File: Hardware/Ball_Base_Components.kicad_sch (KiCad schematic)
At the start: 58 parts, among them J1 Eurorack_10_pin_power, J2 SWD_Header, J3 USB_B_Micro, J4 X_Out, J5 Y_Out, J6 Z_Out, U1 STM32WB35, U3 LD1117-3.3-4Tab, U4 TL072, U5 TL074, Y2 32MHz

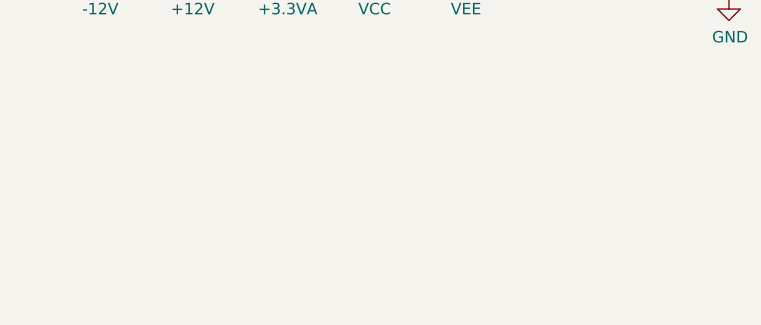
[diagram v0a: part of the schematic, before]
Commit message: Base PCB Updates and resize
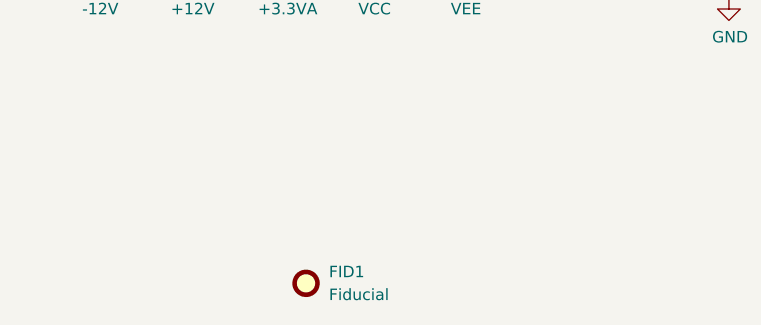
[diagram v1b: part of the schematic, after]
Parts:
- added FID1: Fiducial, Custom_Footprints:4_Layer_Markers, symbol Mechanical:Fiducial
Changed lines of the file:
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@@
     (pin "2")
+  )
+  (symbol (lib_id "Mechanical:Fiducial") (at 44.45 236.22 0) (unit 1)
+    (in_bom yes) (on_board yes) (fields_autoplaced)
+    (property "Reference" "FID1" (id 0) (at 46.99 234.9499 0)
+      (effects (font (size 1.27 1.27)) (justify left))
+    )
+    (property "Value" "Fiducial" (id 1) (at 46.99 237.4899 0)
+      (effects (font (size 1.27 1.27)) (justify left))
+    )
+    (property "Footprint" "Custom_Footprints:4_Layer_Markers" (id 2) (at 44.45 236.22 0)
+      (effects (font (size 1.27 1.27)) hide)
+    )
+    (property "Datasheet" "~" (id 3) (at 44.45 236.22 0)
+      (effects (font (size 1.27 1.27)) hide)
+    )
   )
   (symbol (lib_id "Eurorack_Header:Eurorack_10_pin_power") (at 52.07 170.18 180) (unit 1)
@@
       (reference "D6") (unit 1) (value "LED_BLUE") (footprint "LED_THT:LED_D3.0mm_FlatTop")
     )
+    (path "/04f2824f-3443-40bb-8214-5d853124bdb4"
+      (reference "FID1") (unit 1) (value "Fiducial") (footprint "Custom_Footprints:4_Layer_Markers")
+    )
     (path "/06d56cea-efec-4ee2-a30e-da196d83ccb4"

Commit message: Base - started panel PCB
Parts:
- added C13, C17: 100nF, Capacitor_SMD:C_0603_1608Metric, symbol Device:C_Small
- added CONNECT1: SW_Push, Button_Switch_THT:SW_Tactile_SPST_Angled_PTS645Vx58-2LFS, symbol Switch:SW_Push
- added TP1, TP2, TP3, TP4: TestPoint, Custom_Footprints:1.3mm_Test_Point, symbol Connector:TestPoint
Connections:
- net +3V3: now also TP2.1
- net GND: now also C13.1, C17.1, CONNECT1.2, TP1.1
- net VCC: now also C13.2, TP3.1
- net VEE: now also C17.2, TP4.1
- net CONNECT: now reaches U1.13 (PA4)
- net CONNECT: now also CONNECT1.1
- no-connect marks 28 -> 27
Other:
- moved on the sheet: U4C

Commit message: Minor PCB Updates
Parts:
- FID1: value Fiducial -> 4 Layer Marker
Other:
- note added: "Connectors/Buttons"
- note added: "LEDs"
- note added: "MCU"
- note added: "PWM Filtering"
- note added: "Power"
- company: (none) -> Mountjoy Modular
- title: (none) -> Ball Base Unit
- moved on the sheet: AE1, C1, C10, C11, C12, C13, C14, C15, C16, C17, C19, C2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

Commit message: More PCB Clean up
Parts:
- renumbered C3 to C1, C11 to C10, C12 to C11, C14 to C12, C15 to C13, C16 to C14, C17 to C15, C13 to C16, C2 to C17, C1 to C18, C21 to C19, C4 to C2, C19 to C20, C22 to C21, C20 to C22, C5 to C3, C7 to C4, C25 to C5, C9 to C6, C10 to C7, C6 to C8, C8 to C9, D6 to D3, D3 to D4, D4 to D5, D5 to D6, R5 to R1, R12 to R11, R16 to R12, R14 to R13, R6 to R14, R7 to R15, R8 to R16, R1 to R2, R2 to R3, R3 to R5, R9 to R6, R11 to R7, R15 to R8, R13 to R9, U3 to U2, U5 to U3, Y2 to Y1
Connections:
- net Y_Filtered: now also U3.12 (+); no longer U4.3 (+)
- net Z_Filtered: now also U4.3 (+); no longer U3.12 (+)
- net at D5.1 (K), R15.2: now also U3.13 (-); no longer U4.2 (-)
- net at D5.2 (A): now also U3.14; no longer U4.1
- net at D6.1 (K), R16.2: now also U4.2 (-); no longer U3.13 (-)
- net at D6.2 (A): now also U4.1; no longer U3.14
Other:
- moved on the sheet: U3D, U4A

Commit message: PCB Updates
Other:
- moved on the sheet: AE1, C1, C12, C13, C17, C18, C19, C2, C20, C21, C22, C3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

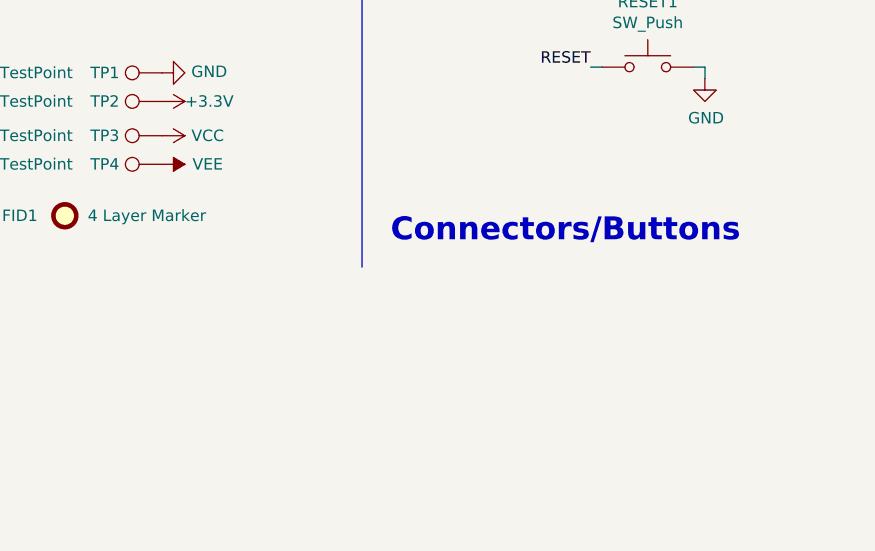
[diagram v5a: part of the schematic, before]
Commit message: Created test firmware for STM32WB35 hardware (not yet working)
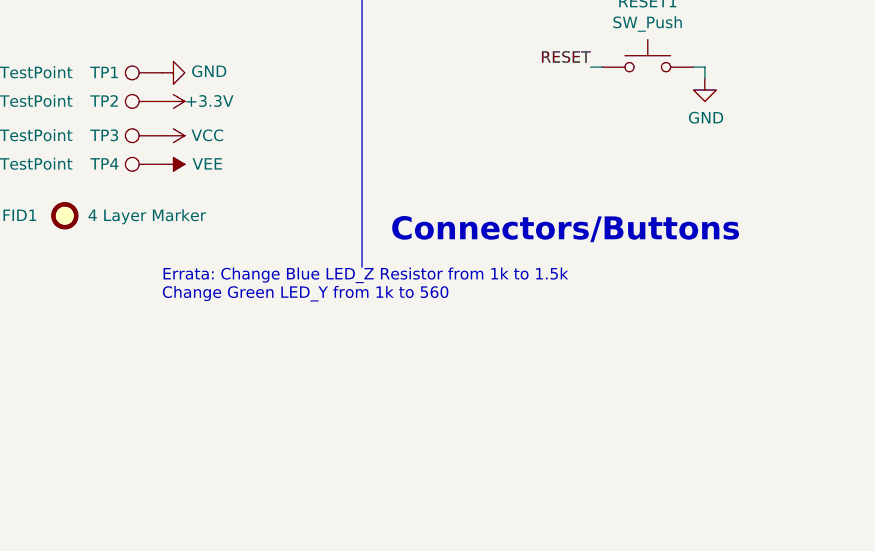
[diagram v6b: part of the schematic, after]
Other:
- note added: "Errata: Change Blue LED_Z Resistor from 1k to 1.5k Change Green LED_Y from 1k to 560"
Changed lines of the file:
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@@
     (effects (font (size 2.54 2.54) (thickness 0.508) bold) (justify left bottom))
+  )
+  (text "Errata: Change Blue LED_Z Resistor from 1k to 1.5k\nChange Green LED_Y from 1k to 560"
+    (at 222.25 199.39 0)
+    (effects (font (size 1.27 1.27)) (justify left bottom))
   )
   (text "Power" (at 14.605 224.155 0)
@@
       (effects (font (size 1.27 1.27)) hide)
     )
+    (pin "1")
+    (pin "2")
+    (pin "3")
+    (pin "5")
+    (pin "6")
+    (pin "7")
+    (pin "10")
+    (pin "8")
+    (pin "9")
+    (pin "12")
+    (pin "13")
+    (pin "14")
     (pin "11")
     (pin "4")
@@
       (effects (font (size 1.27 1.27)) hide)
     )
+    (pin "1")
+    (pin "2")
+    (pin "3")
     (pin "5")
     (pin "6")
     (pin "7")
+    (pin "4")
+    (pin "8")
   )
   (symbol (lib_id "Device:C_Small") (at 49.53 136.525 0) (unit 1)
@@
     (pin "2")
     (pin "3")
+    (pin "5")
+    (pin "6")
+    (pin "7")
+    (pin "10")
+    (pin "8")
+    (pin "9")
+    (pin "12")
+    (pin "13")
+    (pin "14")
+    (pin "11")
+    (pin "4")
   )
   (symbol (lib_id "power:PWR_FLAG") (at 179.07 183.515 90) (unit 1)
@@
       (effects (font (size 1.27 1.27)) hide)
     )
+    (pin "1")
+    (pin "2")
+    (pin "3")
+    (pin "5")
+    (pin "6")
+    (pin "7")
     (pin "10")
     (pin "8")
     (pin "9")
+    (pin "12")
+    (pin "13")
+    (pin "14")
+    (pin "11")
+    (pin "4")
   )
   (symbol (lib_id "power:+12V") (at 35.56 188.595 90) (unit 1)
@@
       (effects (font (size 1.27 1.27)) hide)
     )
+    (pin "1")
+    (pin "2")
+    (pin "3")
+    (pin "5")
+    (pin "6")
+    (pin "7")
+    (pin "10")
+    (pin "8")
+    (pin "9")
     (pin "12")
     (pin "13")
     (pin "14")
+    (pin "11")
+    (pin "4")
   )
   (symbol (lib_id "Device:R_Small") (at 43.815 72.39 90) (unit 1)
@@
       (effects (font (size 1.27 1.27)) hide)
     )
+    (pin "1")
+    (pin "2")
+    (pin "3")
     (pin "5")
     (pin "6")
     (pin "7")
+    (pin "10")
+    (pin "8")
+    (pin "9")
+    (pin "12")
+    (pin "13")
+    (pin "14")
+    (pin "11")
+    (pin "4")
   )
   (symbol (lib_id "Device:R_Small") (at 146.05 93.345 180) (unit 1)
@@
       (effects (font (size 1.27 1.27)) hide)
     )
+    (pin "1")
+    (pin "2")
+    (pin "3")
+    (pin "5")
+    (pin "6")
+    (pin "7")
     (pin "4")
     (pin "8")
@@
     (pin "2")
     (pin "3")
+    (pin "5")
+    (pin "6")
+    (pin "7")
+    (pin "4")
+    (pin "8")
   )
   (symbol (lib_id "Switch:SW_Push") (at 276.225 156.21 0) (unit 1)
